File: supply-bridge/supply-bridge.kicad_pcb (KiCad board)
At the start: 2 copper layers, 57.8 x 5.1 mm, 4 parts, among them P1 CONN_1X1, P2 CONN_1X1, P3 CONN_1X1, P4 CONN_1X1

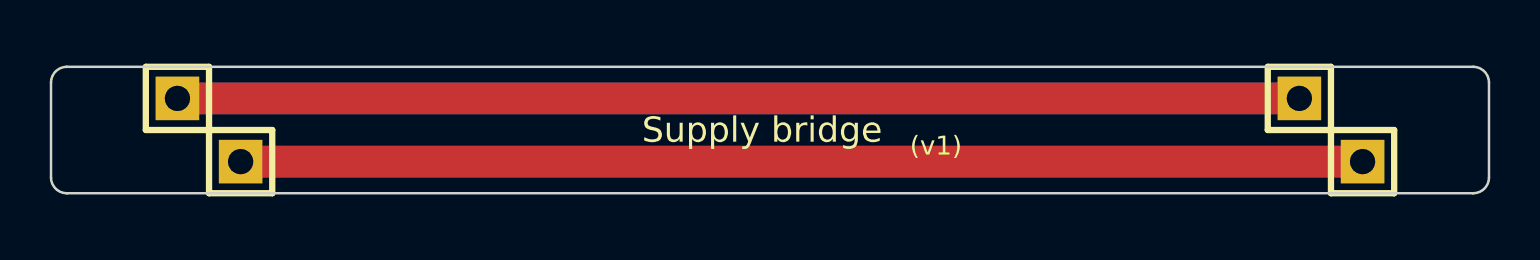
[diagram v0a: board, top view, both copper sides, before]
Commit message: minimum OSHPark board width is 0.25 inches
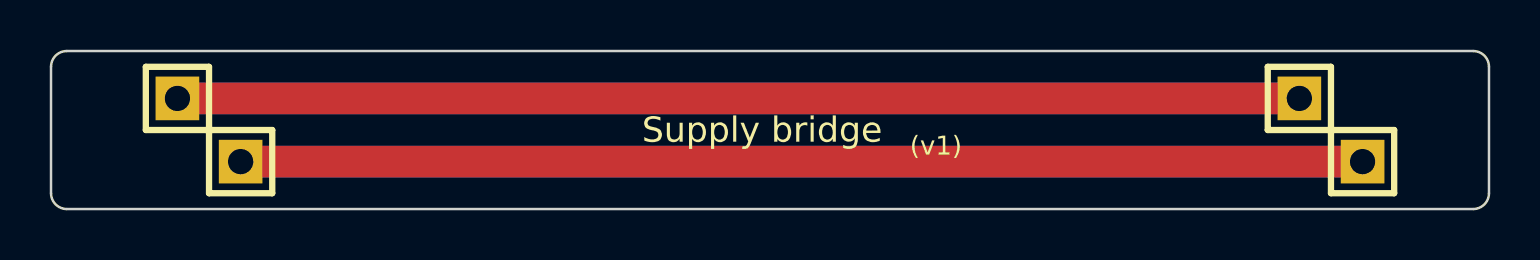
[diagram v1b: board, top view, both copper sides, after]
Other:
- board size 57.8 x 5.1 mm -> 57.8 x 6.3 mm
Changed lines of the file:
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@@
     )
   )
+  (gr_line (start 280.67 125.095) (end 224.155 125.095) (angle 90) (layer Edge.Cuts) (width 0.1))
+  (gr_line (start 281.305 130.81) (end 281.305 125.73) (angle 90) (layer Edge.Cuts) (width 0.1))
+  (gr_line (start 224.155 131.445) (end 280.67 131.445) (angle 90) (layer Edge.Cuts) (width 0.1))
+  (gr_line (start 223.52 125.73) (end 223.52 130.81) (angle 90) (layer Edge.Cuts) (width 0.1))
   (gr_text "(v1)" (at 259.08 128.905) (layer F.SilkS)
     (effects (font (size 0.762 0.762) (thickness 0.1524)))
@@
     (effects (font (size 1.016 1.016) (thickness 0.2032)))
   )
-  (gr_line (start 280.67 130.81) (end 224.155 130.81) (angle 90) (layer Edge.Cuts) (width 0.1))
-  (gr_line (start 224.155 125.73) (end 280.67 125.73) (angle 90) (layer Edge.Cuts) (width 0.1))
-  (gr_line (start 223.52 126.365) (end 223.52 130.175) (angle 90) (layer Edge.Cuts) (width 0.1))
-  (gr_line (start 281.305 126.365) (end 281.305 130.175) (angle 90) (layer Edge.Cuts) (width 0.1))
-  (gr_arc (start 280.67 126.365) (end 280.67 125.73) (angle 90) (layer Edge.Cuts) (width 0.1))
-  (gr_arc (start 280.67 130.175) (end 281.305 130.175) (angle 90) (layer Edge.Cuts) (width 0.1))
-  (gr_arc (start 224.155 130.175) (end 224.155 130.81) (angle 90) (layer Edge.Cuts) (width 0.1))
-  (gr_arc (start 224.155 126.365) (end 223.52 126.365) (angle 90) (layer Edge.Cuts) (width 0.1))
+  (gr_arc (start 280.67 125.73) (end 280.67 125.095) (angle 90) (layer Edge.Cuts) (width 0.1))
+  (gr_arc (start 280.67 130.81) (end 281.305 130.81) (angle 90) (layer Edge.Cuts) (width 0.1))
+  (gr_arc (start 224.155 130.81) (end 224.155 131.445) (angle 90) (layer Edge.Cuts) (width 0.1))
+  (gr_arc (start 224.155 125.73) (end 223.52 125.73) (angle 90) (layer Edge.Cuts) (width 0.1))
   (segment (start 231.14 129.54) (end 276.225 129.54) (width 1.27) (layer F.Cu) (net 1))
   (segment (start 231.14 129.54) (end 276.225 129.54) (width 1.27) (layer B.Cu) (net 1))
